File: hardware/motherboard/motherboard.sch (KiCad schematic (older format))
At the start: 2 parts, among them P1 Conn_02x20_Odd_Even

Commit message: work on hardware motherboard
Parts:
- added C1, C2, C3, C4: 10µF, Capacitor_THT:CP_Radial_D6.3mm_P2.50mm, symbol Device:CP
- added C10, C12, C13, C14: 1000µF, Capacitor_THT:CP_Radial_D10.0mm_P5.00mm, symbol Device:CP
- added C11, C15, C16, C9: 100nF, Capacitor_THT:C_Disc_D5.0mm_W2.5mm_P5.00mm, symbol Device:C
- added C5, C7: 8n2, Capacitor_THT:C_Disc_D5.0mm_W2.5mm_P5.00mm, symbol Device:C
- added C6, C8: 470µF, Capacitor_THT:CP_Radial_D10.0mm_P5.00mm, symbol Device:CP
- added J1: Conn_01x04_Female, Connector_PinSocket_2.54mm:PinSocket_1x04_P2.54mm_Vertical, symbol Connector:Conn_01x04_Female
- added J10, J11, J8: Conn_01x02_Female, TerminalBlock:TerminalBlock_bornier-2_P5.08mm, symbol Connector:Conn_01x02_Female
- added J2: AudioJack3_Ground, Connector_Audio:Jack_3.5mm_CUI_SJ-3523-SMT_Horizontal, symbol Connector:AudioJack3_Ground
- added J4: Conn_01x05_Female, Connector_TE-Connectivity:TE_826576-5_1x05_P3.96mm_Vertical, symbol Connector:Conn_01x05_Female
- added J5, J6, J7: Conn_01x05_Female, Connector_PinSocket_2.54mm:PinSocket_1x05_P2.54mm_Vertical, symbol Connector:Conn_01x05_Female
- added J9: Conn_01x03_Female, TerminalBlock:TerminalBlock_bornier-3_P5.08mm, symbol Connector:Conn_01x03_Female
- added K1: SANYOU_SRD_Form_A, Relay_THT:Relay_SPST_SANYOU_SRD_Series_Form_A, symbol Relay:SANYOU_SRD_Form_A
- added K2: SANYOU_SRD_Form_C, Relay_THT:Relay_SPDT_SANYOU_SRD_Series_Form_C, symbol Relay:SANYOU_SRD_Form_C
- added Q1, Q2, Q3: BSS138, Package_TO_SOT_SMD:SOT-23, symbol Transistor_FET:BSS138
- added R1, R15, R2, R3, R4, R5, R6: 10K, Resistor_THT:R_Axial_DIN0207_L6.3mm_D2.5mm_P7.62mm_Horizontal, symbol Device:R
- added R10, R12: 4R7, Resistor_THT:R_Axial_DIN0207_L6.3mm_D2.5mm_P7.62mm_Horizontal, symbol Device:R
- added R11, R9: 470R, Resistor_THT:R_Axial_DIN0207_L6.3mm_D2.5mm_P7.62mm_Horizontal, symbol Device:R
- added R13, R14: 1R, Resistor_THT:R_Axial_DIN0207_L6.3mm_D2.5mm_P7.62mm_Horizontal, symbol Device:R
- added R7, R8: 100R, Resistor_THT:R_Axial_DIN0207_L6.3mm_D2.5mm_P7.62mm_Horizontal, symbol Device:R
- added RV1, RV2: 10K, Potentiometer_SMD:Potentiometer_Bourns_3314J_Vertical, symbol Device:R_POT
- added U1, U2: TDA2003, Package_TO_SOT_THT:TO-220-5_P3.4x3.7mm_StaggerOdd_Lead3.8mm_Vertical, symbol Amplifier_Audio:TDA2003
- J3: renamed from J?; footprint (none) -> TerminalBlock:TerminalBlock_bornier-5_P5.08mm
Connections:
- net labels added: AMP1_IN, AMP1_LS, AMP2_IN, AMP2_LS, M1, M1_HA, M2, M2_HA, M3, M3_HA, MOTOR_RELAY, MOTOR_SIGNAL, MOTOR_VR, MOTOR_ZF, RTC_SCL, RTC_SDA, SSR_RELAY
- wire segments 62 -> 220
- no-connect marks 0 -> 1
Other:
- note added: "AUDIO AMPLIFIER 1"
- note added: "AUDIO AMPLIFIER 2"
- note added: "CONNECTIONS"
- note added: "ESC"
- note added: "MISC"
- note added: "POWER IN CONNECTORS"
- note added: "RPi GPIO"
- note added: "RTC (DS3231) module"
- moved on the sheet: J3, P1

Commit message: layout of first mb; test print
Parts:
- removed J2: AudioJack3_Ground, Connector_Audio:Jack_3.5mm_CUI_SJ-3523-SMT_Horizontal, symbol Connector:AudioJack3_Ground
- removed J5: Conn_01x05_Female, Connector_PinSocket_2.54mm:PinSocket_1x05_P2.54mm_Vertical, symbol Connector:Conn_01x05_Female
- removed K1: SANYOU_SRD_Form_A, Relay_THT:Relay_SPST_SANYOU_SRD_Series_Form_A, symbol Relay:SANYOU_SRD_Form_A
- removed R2, R5: 10K, Resistor_THT:R_Axial_DIN0207_L6.3mm_D2.5mm_P7.62mm_Horizontal, symbol Device:R
- added C17: 1000µF, Capacitor_THT:CP_Radial_D10.0mm_P5.00mm, symbol Device:CP
- added D1: 1N4148W, Diode_SMD:D_SOD-123, symbol Diode:1N4148W
- added J2: Conn_01x03_Male, Connector_PinHeader_2.54mm:PinHeader_1x03_P2.54mm_Vertical, symbol Connector:Conn_01x03_Male
- added J5: Conn_01x06_Female, Connector_PinSocket_2.54mm:PinSocket_1x06_P2.54mm_Vertical, symbol Connector:Conn_01x06_Female
- added M1, M2: Fan_3pin, Connector:FanPinHeader_1x03_P2.54mm_Vertical, symbol Motor:Fan_3pin
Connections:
- net labels removed: +3.3V, MOTOR_SIGNAL, MOTOR_ZF
- wire segments 220 -> 230
- no-connect marks 1 -> 5
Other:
- moved on the sheet: C1, C10, C11, C12, C13, C14, C15, C16, C2, C3, C4, C5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

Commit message: ordered first version
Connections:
- net M1: now also J9.1 (Pin_1); no longer J9.3 (Pin_3)
- net M3: now also J9.3 (Pin_3); no longer J9.1 (Pin_1)
- net at P1.1 (Pin_1): no longer P1.17 (Pin_17)
- no-connect marks 5 -> 6
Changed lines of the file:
@@
 	2150 2750 2250 2750
 Connection ~ 2150 3450
-Connection ~ 2050 1550
-Wire Wire Line
-	2050 1400 2050 1550
 Wire Wire Line
 	2150 1950 2250 1950
@@
 	2150 3450 2150 3600
 Wire Wire Line
-	2050 1550 2050 2350
-Wire Wire Line
 	2850 2150 2850 2450
 Text Notes 1100 1050 0    79   ~ 0
@@
 F 3 "~" H 6500 2000 50  0001 C CNN
 	1    6500 2000
-	1    0    0    1
+	1    0    0    -1
 $EndComp
 Wire Wire Line
@@
 	2250 2450 1100 2450
 Wire Wire Line
-	2050 1550 2250 1550
-Wire Wire Line
-	2050 2350 2250 2350
-Wire Wire Line
 	1100 2250 2250 2250
 Wire Wire Line
@@
 	2850 1750 3150 1750
 Connection ~ 2850 1750
-NoConn ~ 2050 1400
 $Comp
 L Motor:Fan_3pin M1
@@
 NoConn ~ 4600 9200
 NoConn ~ 3550 9200
+NoConn ~ 2250 1550
+NoConn ~ 2250 2350
 $EndSCHEMATC

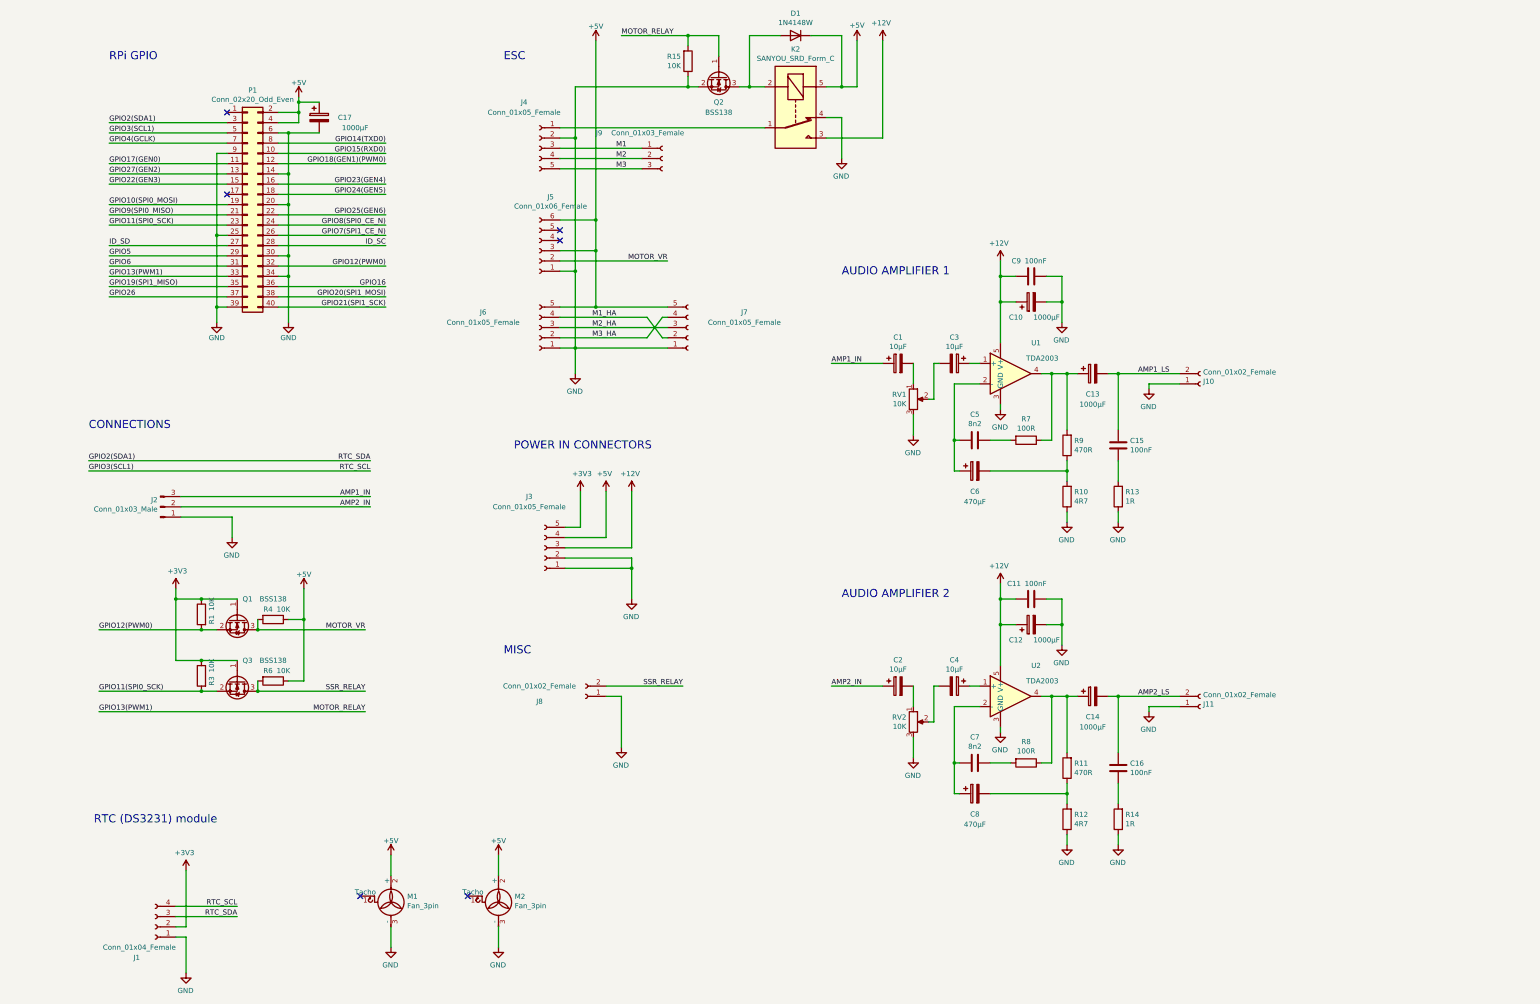
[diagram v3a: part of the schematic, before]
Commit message: added lights to schematic
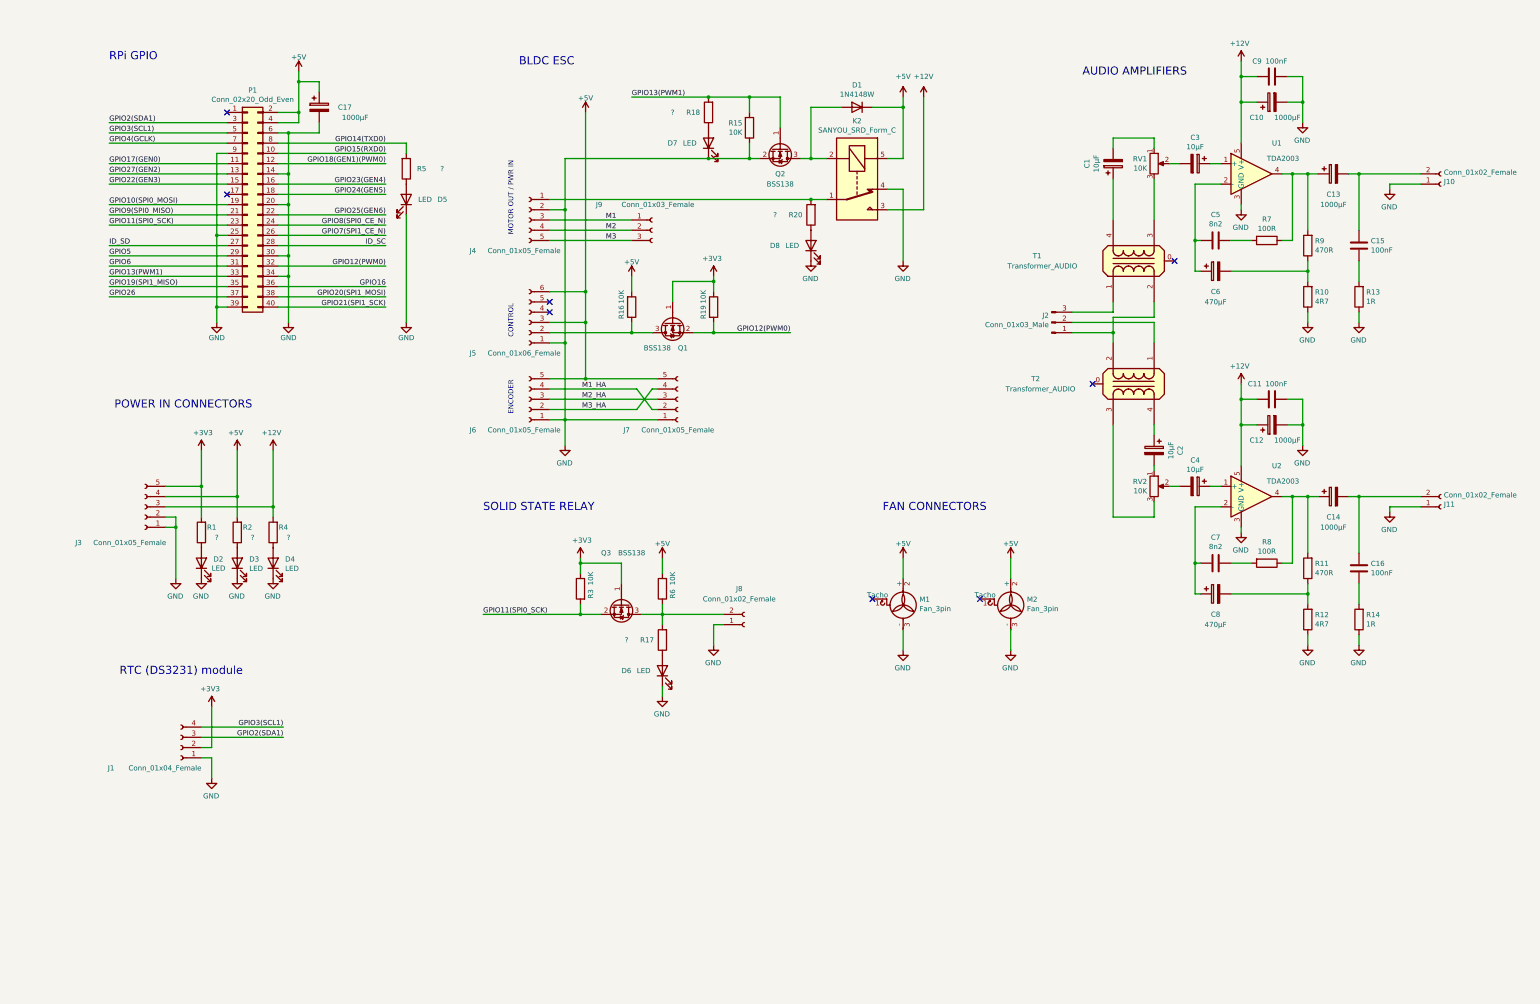
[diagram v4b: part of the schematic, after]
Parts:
- added D2, D3, D4, D5, D6, D7, D8: LED, symbol Device:LED
- added R16, R19: 10K, Resistor_THT:R_Axial_DIN0207_L6.3mm_D2.5mm_P7.62mm_Horizontal, symbol Device:R
- added R17, R18, R2, R20, R5: ?, Resistor_THT:R_Axial_DIN0207_L6.3mm_D2.5mm_P7.62mm_Horizontal, symbol Device:R
- added T1, T2: Transformer_AUDIO, symbol Device:Transformer_AUDIO
- R1, R4: value 10K -> ?
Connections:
- net +12V: now also R4.2
- net +3V3: now also R1.2, R19.1; no longer R1.1
- net +5V: now also R6.2, R16.2, R2.2; no longer R4.1, R6.1
- net GND: now also D2.1 (K), D3.1 (K), D4.1 (K), D5.1 (K), D6.1 (K), D7.1 (K), D8.1 (K); no longer J2.1 (Pin_1), RV1.3, RV2.3
- net GPIO12(PWM0): now also R19.2; no longer R1.2
- net GPIO13(PWM1): now also R18.2
- net GPIO14(TXD0): now also R5.2
- net at J4.1 (Pin_1), K2.1: now also R20.2
- net AMP1_IN: no longer names the net of J2.3 (Pin_3)
- net AMP1_IN: now also T1.1 (AA); no longer C1.1
- net AMP1_LS: no longer names the net of C13.2, C15.1, J10.2 (Pin_2)
- net AMP2_IN: no longer names the net of J2.2 (Pin_2)
- net AMP2_IN: now also T2.1 (AA); no longer C2.1
- net AMP2_LS: no longer names the net of C14.2, C16.1, J11.2 (Pin_2)
- net MOTOR_VR: no longer names the net of J5.2 (Pin_2), Q1.3 (D)
- net MOTOR_VR: now also R16.1; no longer R4.2
- net SSR_RELAY: no longer names the net of J8.2 (Pin_2), Q3.3 (D)
- net SSR_RELAY: now also R6.1, R17.2; no longer R6.2
- new net: D2.2 (A), R1.1
- new net: J2.1 (Pin_1), T1.2 (AB), T2.2 (AB)
- new net: D3.2 (A), R2.1
- new net: D4.2 (A), R4.1
- new net: D7.2 (A), R18.1
- new net: RV2.3, T2.3 (SA)
- new net: C2.1, T2.4 (SB)
- new net: RV1.3, T1.3 (SA)
- new net: C1.1, T1.4 (SB)
- new net: D8.2 (A), R20.1
- new net: D6.2 (A), R17.1
- new net: D5.2 (A), R5.1
- no-connect marks 6 -> 8
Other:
- note added: "AUDIO AMPLIFIERS"
- note added: "BLDC ESC"
- note added: "CONTROL"
- note added: "ENCODER"
- note added: "FAN CONNECTORS"
- note added: "MOTOR OUT / PWR IN"
- note added: "SOLID STATE RELAY"
- note removed: "AUDIO AMPLIFIER 1"
- note removed: "AUDIO AMPLIFIER 2"
- note removed: "CONNECTIONS"
- note removed: "ESC"
- note removed: "MISC"
- moved on the sheet: C10, C11, C12, C13, C14, C15, C16, C17, C2, C3, C4, C5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

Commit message: pcb design v2
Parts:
- removed M1, M2: Fan_3pin, Connector:FanPinHeader_1x03_P2.54mm_Vertical, symbol Motor:Fan_3pin
- removed T1, T2: Transformer_AUDIO, symbol Device:Transformer_AUDIO
- added C18: 1000µF, Capacitor_THT:CP_Radial_D5.0mm_P2.50mm, symbol Device:CP
- added D9: LED, LED_SMD:LED_1210_3225Metric_Pad1.42x2.65mm_HandSolder, symbol Device:LED
- added J12, J13, J14: Conn_01x03_Male, Connector:FanPinHeader_1x03_P2.54mm_Vertical, symbol Connector:Conn_01x03_Male
- added J15: Conn_01x06_Female, Connector_PinSocket_2.54mm:PinSocket_1x06_P2.54mm_Vertical, symbol Connector:Conn_01x06_Female
- added R21: ?, Resistor_SMD:R_1210_3225Metric_Pad1.42x2.65mm_HandSolder, symbol Device:R
- added TR1, TR2: TRANSF5, Local_Transformer_Audio:MURATA_DA10XJ_Audo_Transformer, symbol Transformer:TRANSF5
- C17: footprint Capacitor_THT:CP_Radial_D10.0mm_P5.00mm -> Capacitor_THT:CP_Radial_D5.0mm_P2.50mm
- D1: footprint Diode_SMD:D_SOD-123 -> Diode_SMD:D_SOD-128
- D2, D3, D4, D5, D6, D7, D8: footprint (none) -> LED_SMD:LED_1210_3225Metric_Pad1.42x2.65mm_HandSolder
- Q1, Q2, Q3: footprint Package_TO_SOT_SMD:SOT-23 -> Package_TO_SOT_SMD:SOT-23_Handsoldering
- R1, R10, R11, R12, R13, R14, R15, R16, R17, R18, R19, R2, R20, R3, R4, R5, R6, R7, R8, R9: footprint Resistor_THT:R_Axial_DIN0207_L6.3mm_D2.5mm_P7.62mm_Horizontal -> Resistor_SMD:R_1210_3225Metric_Pad1.42x2.65mm_HandSolder
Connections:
- net +12V: now also J14.2 (Pin_2)
- net +3V3: now also J15.2 (Pin_2); no longer R19.1, R3.1
- net +5V: now also C18.1, J12.2 (Pin_2), J13.2 (Pin_2)
- net GND: now also R19.2, R3.2, C18.2, D9.1 (K), J12.1 (Pin_1), J13.1 (Pin_1), J14.1 (Pin_1), J15.1 (Pin_1)
- net GPIO11(SPI0_SCK): now also R3.1; no longer R3.2
- net GPIO12(PWM0): now also R19.1; no longer R19.2
- net GPIO2(SDA1): now also J15.3 (Pin_3)
- net GPIO3(SCL1): now also J15.4 (Pin_4)
- net at J5.2 (Pin_2), Q1.3 (D), R16.1: now also R21.2
- net at J2.1 (Pin_1): now also TR1.3, TR2.3
- net at J2.2 (Pin_2): now also TR2.1
- net at J2.3 (Pin_3): now also TR1.1
- net at RV2.3: now also TR2.4
- net at C2.1: now also TR2.6
- net at RV1.3: now also TR1.4
- net at C1.1: now also TR1.6
- new net: D9.2 (A), R21.1
- no-connect marks 8 -> 11
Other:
- moved on the sheet: D6, Q1, R16, R17, R19, R3, R6
